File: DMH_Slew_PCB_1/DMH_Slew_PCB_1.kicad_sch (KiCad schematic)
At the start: 0 parts

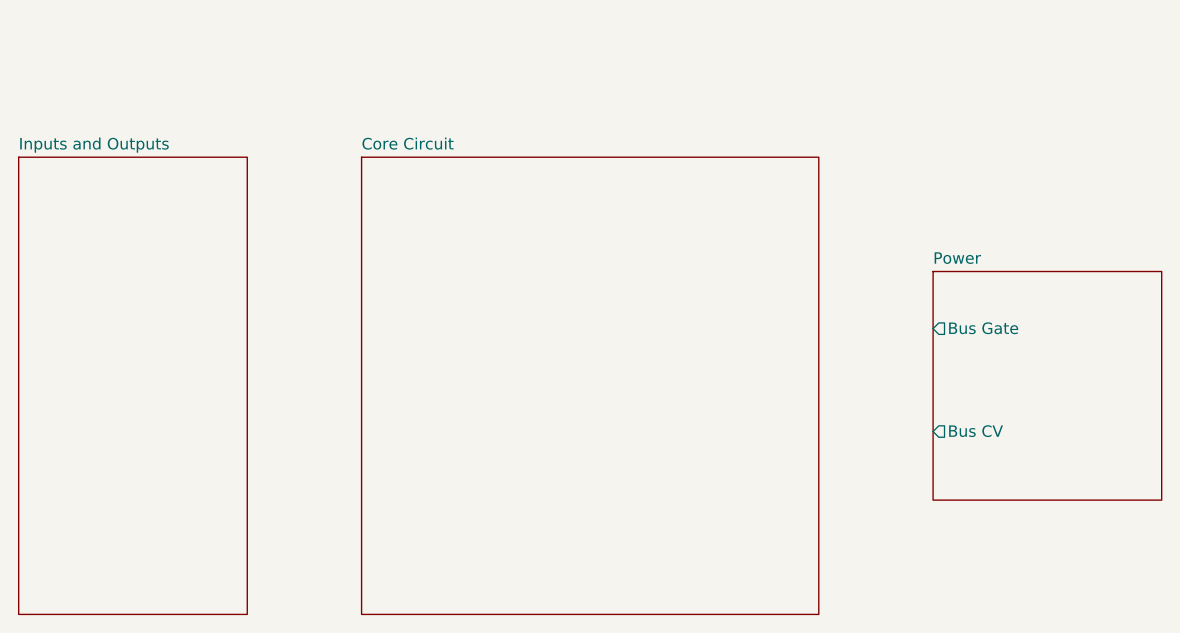
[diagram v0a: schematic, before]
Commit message: Designed IO page
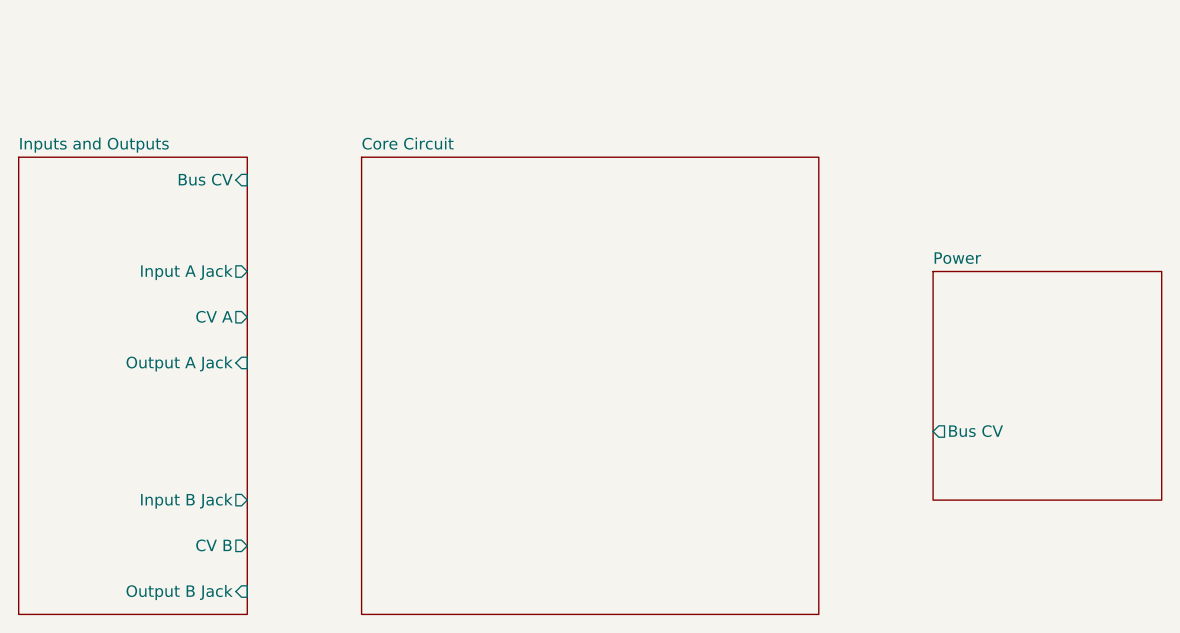
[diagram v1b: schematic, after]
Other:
- sheet Inputs and Outputs ports: added Bus CV, CV A, CV B, Input A Jack, Input B Jack, Output A Jack, Output B Jack; removed none
- sheet Power ports: added none; removed Bus Gate
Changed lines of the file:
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@@
-			)
-		)
-		(pin "Bus Gate" output
-			(at 127 95.25 180)
-			(effects
-				(font
-					(size 1.27 1.27)
-				)
-				(justify left)
 			)
 		)
@@
 		)
 		(instances
-			(project "DMH-Kosmo-5cm-PCB"
+			(project "DMH_Slew_PCB_1"
 				(path "/58f4306d-5387-4983-bb08-41a2313fd315"
 					(page "4")
@@
 		)
 		(instances
-			(project "DMH-Kosmo-5cm-PCB"
+			(project "DMH_Slew_PCB_1"
 				(path "/58f4306d-5387-4983-bb08-41a2313fd315"
 					(page "3")
@@
 			)
 		)
+		(pin "Bus CV" input
+			(at 50.8 78.74 0)
+			(effects
+				(font
+					(size 1.27 1.27)
+				)
+				(justify right)
+			)
+		)
+		(pin "CV A" output
+			(at 50.8 93.98 0)
+			(effects
+				(font
+					(size 1.27 1.27)
+				)
+				(justify right)
+			)
+		)
+		(pin "CV B" output
+			(at 50.8 119.38 0)
+			(effects
+				(font
+					(size 1.27 1.27)
+				)
+				(justify right)
+			)
+		)
+		(pin "Input A Jack" output
+			(at 50.8 88.9 0)
+			(effects
+				(font
+					(size 1.27 1.27)
+				)
+				(justify right)
+			)
+		)
+		(pin "Input B Jack" output
+			(at 50.8 114.3 0)
+			(effects
+				(font
+					(size 1.27 1.27)
+				)
+				(justify right)
+			)
+		)
+		(pin "Output A Jack" input
+			(at 50.8 99.06 0)
+			(effects
+				(font
+					(size 1.27 1.27)
+				)
+				(justify right)
+			)
+		)
+		(pin "Output B Jack" input
+			(at 50.8 124.46 0)
+			(effects
+				(font
+					(size 1.27 1.27)
+				)
+				(justify right)
+			)
+		)
 		(instances
-			(project "DMH-Kosmo-5cm-PCB"
+			(project "DMH_Slew_PCB_1"
 				(path "/58f4306d-5387-4983-bb08-41a2313fd315"
 					(page "2")

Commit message: Schematic design in progress
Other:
- sheet Core Circuit renamed Core Circuit A
- added sheet Core Circuit B (Core_Circuit_B.kicad_sch)
- sheet Core Circuit A: file Core_Circuit.kicad_sch -> Core_Circuit_A.kicad_sch
- sheet Core Circuit A ports: added A Fall CV, A Fall Pot, A Rise CV, A Rise Pot, Input A, Output A; removed none
- sheet Inputs and Outputs ports: added A Fall CV, A Fall Pot, A Rise CV, A Rise Pot, B Fall CV, B Fall Pot, B Rise CV, B Rise Pot; removed CV A, CV B
